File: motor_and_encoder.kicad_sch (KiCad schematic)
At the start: 5 parts, among them J5_1 Conn_02x03_Odd_Even, J5_2 Conn_02x03_Odd_Even, U5_1 DRV8835DSSR

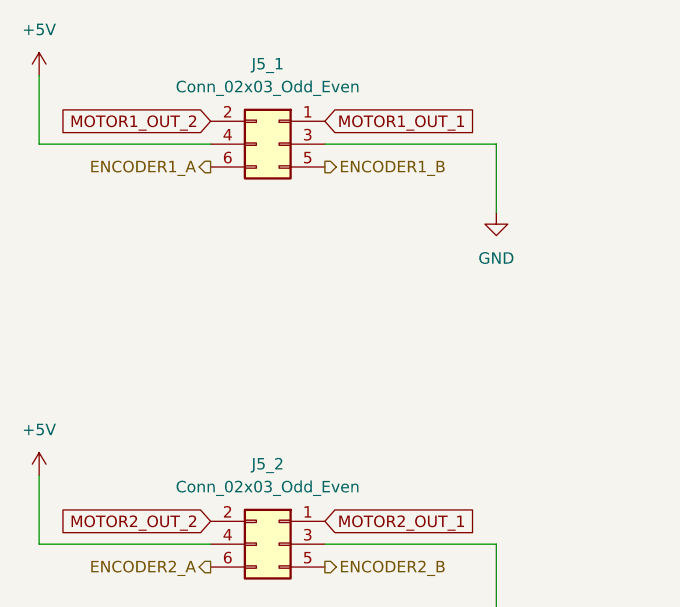
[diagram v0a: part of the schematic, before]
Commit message: エンコーダに型番表記追加
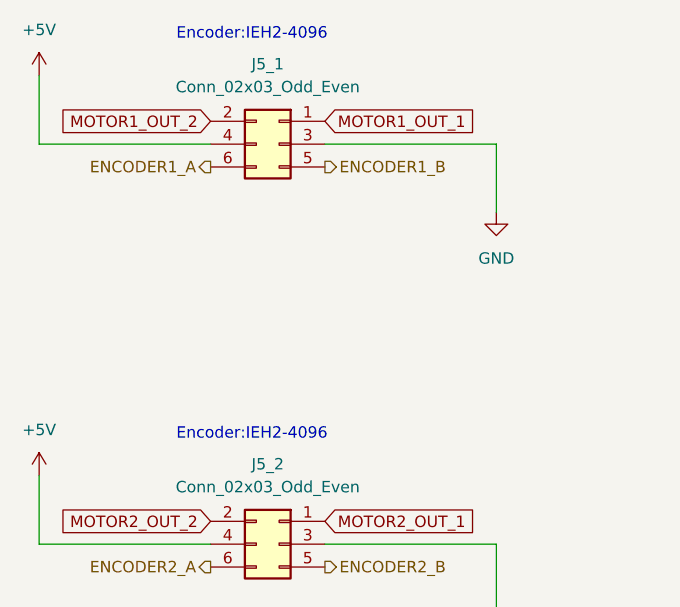
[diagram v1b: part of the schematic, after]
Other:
- note added: "Encoder:IEH2-4096"
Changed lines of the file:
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@@
     (stroke (width 0) (type default))
+  )
+  (text "Encoder:IEH2-4096" (at 73.66 60.96 0)
+    (effects (font (size 1.27 1.27)) (justify left bottom))
   )
   (text "Mode:1(PHASE/ENABLE)" (at 195.58 91.44 0)
     (effects (font (size 1.27 1.27)) (justify left bottom))
   )
+  (text "Encoder:IEH2-4096" (at 73.66 105.41 0)
+    (effects (font (size 1.27 1.27)) (justify left bottom))
+  )

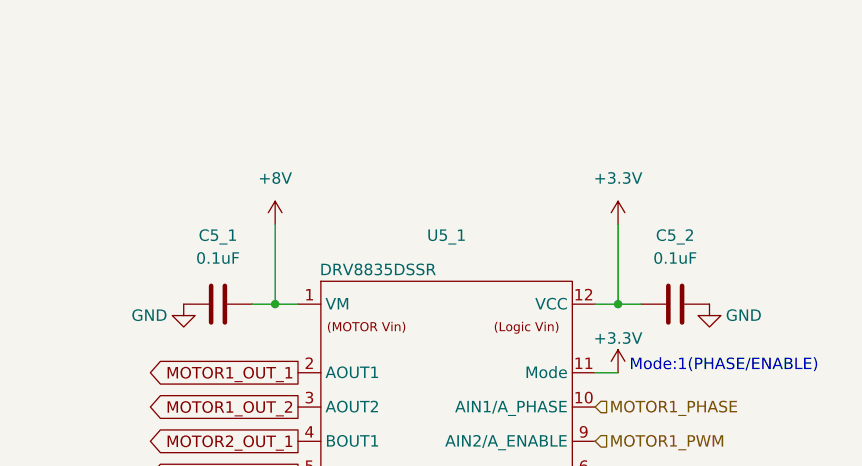
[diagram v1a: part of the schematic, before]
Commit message: モータドライバのVMに対して10uFのコンデンサ追加（10uFの値は秋月のモジュールを参考）
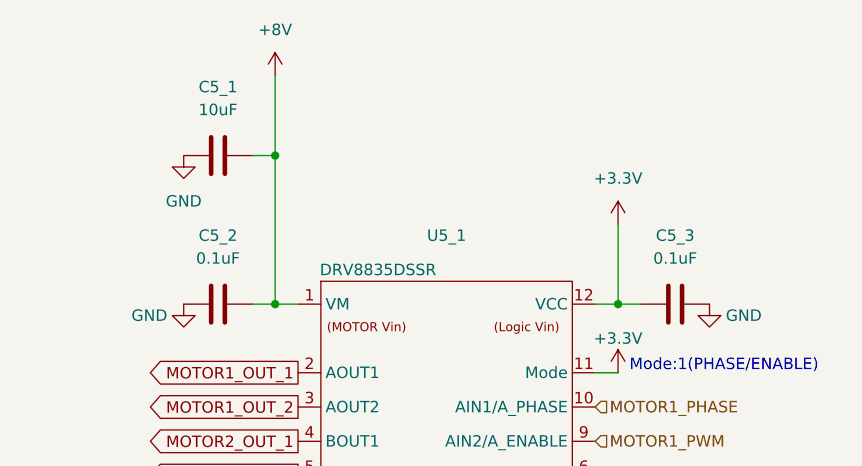
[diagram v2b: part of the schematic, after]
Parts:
- added C5_1: 10uF, symbol Device:C
- renumbered C5_1 to C5_2, C5_2 to C5_3
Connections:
- net +8V: now also C5_1.2
- net GND: now also C5_1.1
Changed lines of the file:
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@@
   (junction (at 194.31 83.82) (diameter 0) (color 0 0 0 0)
   )
+  (junction (at 156.21 67.31) (diameter 0) (color 0 0 0 0)
+  )
   (wire (pts (xy 194.31 74.93) (xy 194.31 83.82))
     (stroke (width 0) (type default))
@@
     (stroke (width 0) (type default))
   )
-  (wire (pts (xy 156.21 74.93) (xy 156.21 83.82))
+  (wire (pts (xy 156.21 58.42) (xy 156.21 67.31))
     (stroke (width 0) (type default))
   )
@@
     (stroke (width 0) (type default))
   )
+  (wire (pts (xy 153.67 67.31) (xy 156.21 67.31))
+    (stroke (width 0) (type default))
+  )
   (wire (pts (xy 196.85 83.82) (xy 194.31 83.82))
     (stroke (width 0) (type default))
@@
   )
   (wire (pts (xy 109.22 116.84) (xy 90.17 116.84))
+    (stroke (width 0) (type default))
+  )
+  (wire (pts (xy 156.21 67.31) (xy 156.21 83.82))
     (stroke (width 0) (type default))
   )
@@
   )
   (symbol (lib_id "Device:C") (at 149.86 83.82 270) (unit 1)
-    (in_bom yes) (on_board yes) (dnp no) (fields_autoplaced)
-    (property "Reference" "C5_1" (at 149.86 76.2 90)
+    (in_bom yes) (on_board yes) (dnp no)
+    (property "Reference" "C5_2" (at 149.86 76.2 90)
       (effects (font (size 1.27 1.27)))
     )
@@
       (project "fast_respect"
         (path "/588ca8cd-b11b-4b55-96d9-278aac6cd0cf/3d29964c-a327-44ac-972f-0ff4ec56671e"
-          (reference "C5_1") (unit 1)
+          (reference "C5_2") (unit 1)
         )
       )
@@
   (symbol (lib_id "Device:C") (at 200.66 83.82 270) (unit 1)
     (in_bom yes) (on_board yes) (dnp no) (fields_autoplaced)
-    (property "Reference" "C5_2" (at 200.66 76.2 90)
+    (property "Reference" "C5_3" (at 200.66 76.2 90)
       (effects (font (size 1.27 1.27)))
     )
@@
       (project "fast_respect"
         (path "/588ca8cd-b11b-4b55-96d9-278aac6cd0cf/3d29964c-a327-44ac-972f-0ff4ec56671e"
-          (reference "C5_2") (unit 1)
+          (reference "C5_3") (unit 1)
         )
       )
@@
     )
   )
+  (symbol (lib_id "power:GND") (at 146.05 67.31 0) (unit 1)
+    (in_bom yes) (on_board yes) (dnp no) (fields_autoplaced)
+    (property "Reference" "#PWR01" (at 146.05 73.66 0)
+      (effects (font (size 1.27 1.27)) hide)
+    )
+    (property "Value" "GND" (at 146.05 72.39 0)
+      (effects (font (size 1.27 1.27)))
+    )
+    (property "Footprint" "" (at 146.05 67.31 0)
+      (effects (font (size 1.27 1.27)) hide)
+    )
+    (property "Datasheet" "" (at 146.05 67.31 0)
+      (effects (font (size 1.27 1.27)) hide)
+    )
+    (pin "1")
+    (instances
+      (project "fast_respect"
+        (path "/588ca8cd-b11b-4b55-96d9-278aac6cd0cf/3d29964c-a327-44ac-972f-0ff4ec56671e"
+          (reference "#PWR01") (unit 1)
+        )
+      )
+    )
+  )
   (symbol (lib_id "power:GND") (at 109.22 80.01 0) (unit 1)
     (in_bom yes) (on_board yes) (dnp no) (fields_autoplaced)
@@
     )
   )
-  (symbol (lib_id "power:+8V") (at 156.21 74.93 0) (unit 1)
+  (symbol (lib_id "Device:C") (at 149.86 67.31 90) (unit 1)
+    (in_bom yes) (on_board yes) (dnp no)
+    (property "Reference" "C5_1" (at 149.86 59.69 90)
+      (effects (font (size 1.27 1.27)))
+    )
+    (property "Value" "10uF" (at 149.86 62.23 90)
+      (effects (font (size 1.27 1.27)))
+    )
+    (property "Footprint" "" (at 153.67 66.3448 0)
+      (effects (font (size 1.27 1.27)) hide)
+    )
+    (property "Datasheet" "~" (at 149.86 67.31 0)
+      (effects (font (size 1.27 1.27)) hide)
+    )
+    (pin "1")
+    (pin "2")
+    (instances
+      (project "fast_respect"
+        (path "/588ca8cd-b11b-4b55-96d9-278aac6cd0cf/3d29964c-a327-44ac-972f-0ff4ec56671e"
+          (reference "C5_1") (unit 1)
+        )
+      )
+    )
+  )
+  (symbol (lib_id "power:+8V") (at 156.21 58.42 0) (unit 1)
     (in_bom yes) (on_board yes) (dnp no) (fields_autoplaced)
-    (property "Reference" "#PWR036" (at 156.21 78.74 0)
-      (effects (font (size 1.27 1.27)) hide)
-    )
-    (property "Value" "+8V" (at 156.21 69.85 0)
-      (effects (font (size 1.27 1.27)))
-    )
-    (property "Footprint" "" (at 156.21 74.93 0)
-      (effects (font (size 1.27 1.27)) hide)
-    )
-    (property "Datasheet" "" (at 156.21 74.93 0)
-      (effects (font (size 1.27 1.27)) hide)
-    )
+    (property "Reference" "#PWR036" (at 156.21 62.23 0)
+      (effects (font (size 1.27 1.27)) hide)
+    )
+    (property "Value" "+8V" (at 156.21 53.34 0)
+      (effects (font (size 1.27 1.27)))
+    )
+    (property "Footprint" "" (at 156.21 58.42 0)
+      (effects (font (size 1.27 1.27)) hide)
+    )
+    (property "Datasheet" "" (at 156.21 58.42 0)
+      (effects (font (size 1.27 1.27)) hide)
+    )

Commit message: アノテーション番号ミスの修正とフットプリント割り当て途中（部品リストも途中生成）
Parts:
- C5_1, C5_2, C5_3: footprint (none) -> Capacitor_SMD:C_0603_1608Metric_Pad1.08x0.95mm_HandSolder
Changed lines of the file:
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@@
       (effects (font (size 1.27 1.27)))
     )
-    (property "Footprint" "" (at 146.05 84.7852 0)
+    (property "Footprint" "Capacitor_SMD:C_0603_1608Metric_Pad1.08x0.95mm_HandSolder" (at 146.05 84.7852 0)
       (effects (font (size 1.27 1.27)) hide)
     )
@@
       (effects (font (size 1.27 1.27)))
     )
-    (property "Footprint" "" (at 196.85 84.7852 0)
+    (property "Footprint" "Capacitor_SMD:C_0603_1608Metric_Pad1.08x0.95mm_HandSolder" (at 196.85 84.7852 0)
       (effects (font (size 1.27 1.27)) hide)
     )
@@
       (effects (font (size 1.27 1.27)))
     )
-    (property "Footprint" "" (at 153.67 66.3448 0)
-      (effects (font (size 1.27 1.27)) hide)
-    )
+    (property "Footprint" "Capacitor_SMD:C_0603_1608Metric_Pad1.08x0.95mm_HandSolder" (at 153.67 66.3448 0)
+      (effects (font (size 1.27 1.27)) hide)
+    )

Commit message: ジャイロとモータドライバのフットプリント作成して登録、シンボルと紐付けた。
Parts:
- U5_1: footprint (none) -> Self-Made_Generic_Packages:WSON-12-1EP_ExpandPad_3x2mm_P0.5mm_EP1x2.65
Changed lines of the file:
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@@
       (effects (font (size 1.27 1.27)))
     )
-    (property "Footprint" "" (at 148.59 87.63 0)
+    (property "Footprint" "Self-Made_Generic_Packages:WSON-12-1EP_ExpandPad_3x2mm_P0.5mm_EP1x2.65" (at 148.59 87.63 0)
       (effects (font (size 1.27 1.27)) hide)
     )

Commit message: スイッチ以外のフットプリント割当完了
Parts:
- J5_1, J5_2: footprint (none) -> Connector_IDC:IDC-Header_2x03_P2.54mm_Vertical
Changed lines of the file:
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@@
       (effects (font (size 1.27 1.27)))
     )
-    (property "Footprint" "" (at 85.09 72.39 0)
+    (property "Footprint" "Connector_IDC:IDC-Header_2x03_P2.54mm_Vertical" (at 85.09 72.39 0)
       (effects (font (size 1.27 1.27)) hide)
     )
@@
       (effects (font (size 1.27 1.27)))
     )
-    (property "Footprint" "" (at 85.09 116.84 0)
+    (property "Footprint" "Connector_IDC:IDC-Header_2x03_P2.54mm_Vertical" (at 85.09 116.84 0)
       (effects (font (size 1.27 1.27)) hide)
     )
